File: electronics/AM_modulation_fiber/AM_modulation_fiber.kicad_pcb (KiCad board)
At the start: 2 copper layers, 88.9 x 70.1 mm, 4 parts

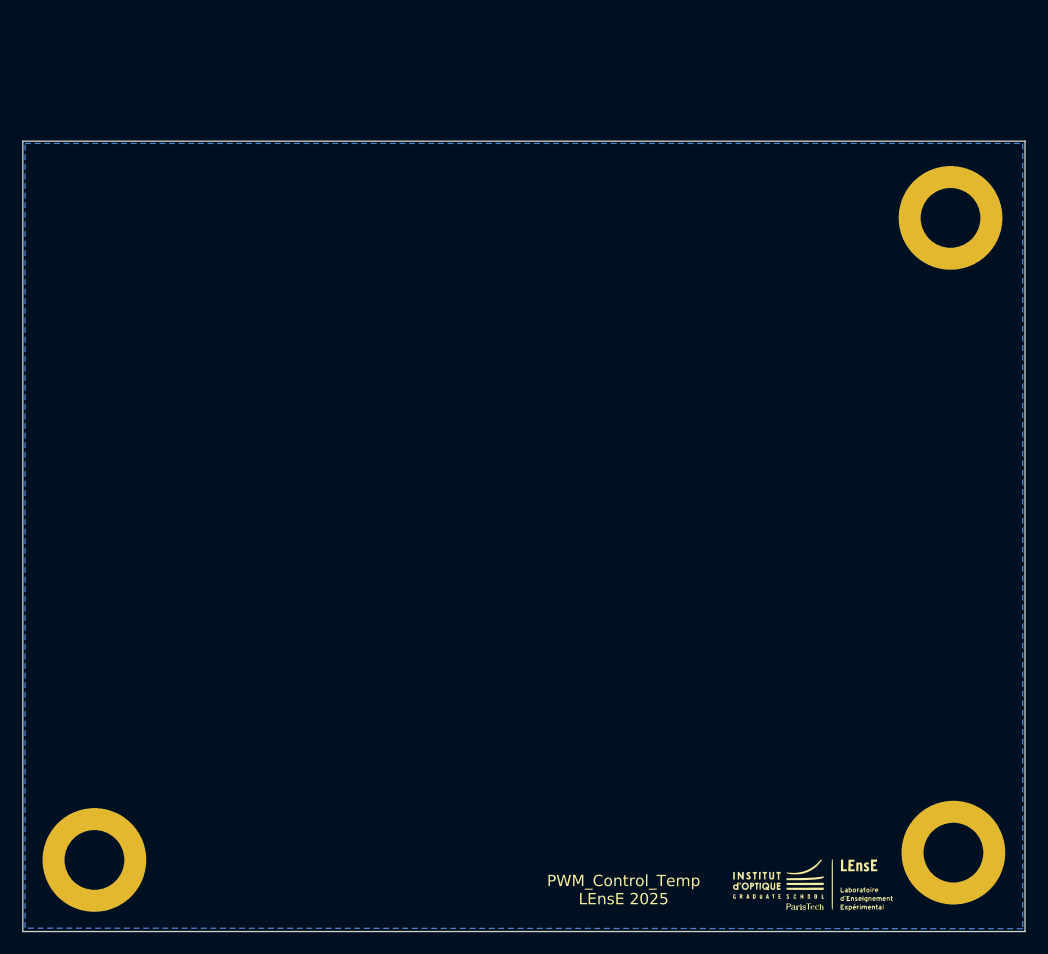
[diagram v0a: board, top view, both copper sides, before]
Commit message: Update AM Modulation and Fiber transmission / demo and labwork
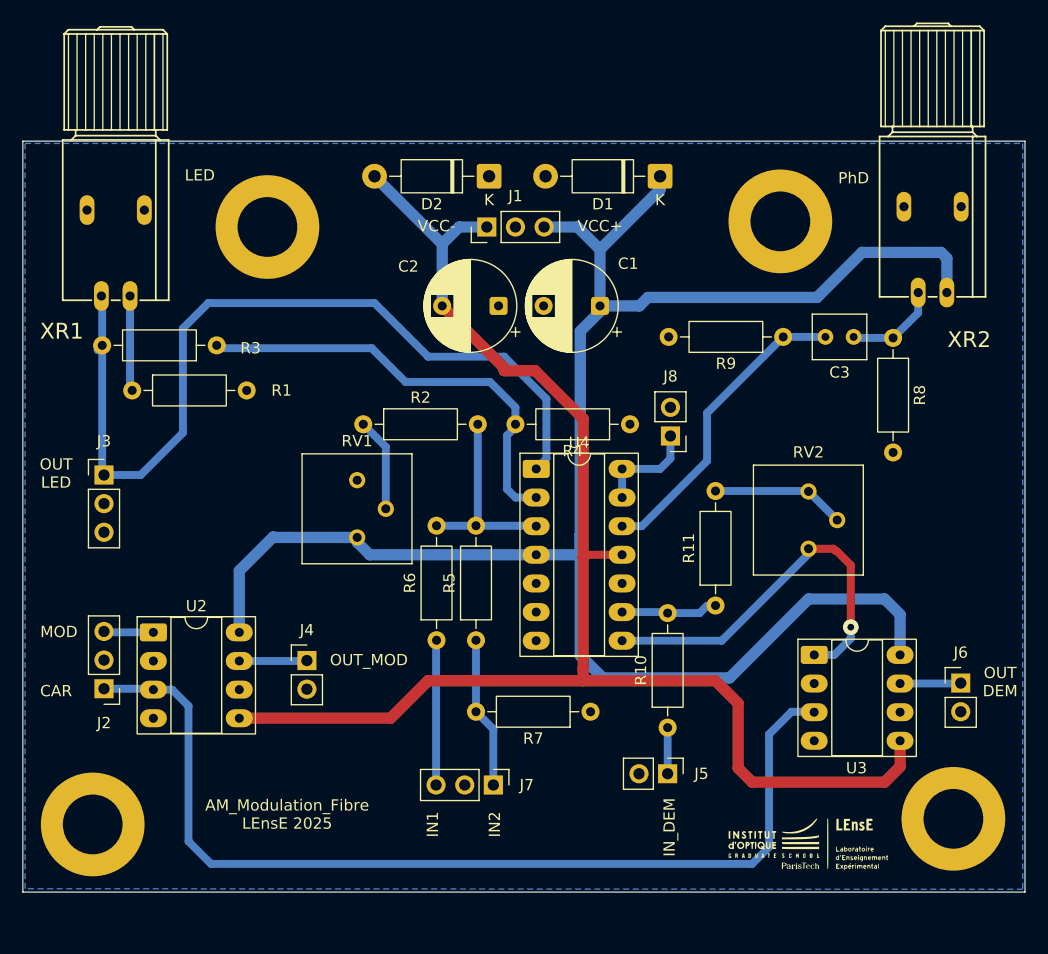
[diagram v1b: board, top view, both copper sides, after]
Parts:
- added ?: , , F.Cu at (199.5, 92.5)
- added C1: 10u, Capacitor_THT:CP_Radial_D8.0mm_P5.00mm, F.Cu at (229.0, 99.5)
- added C2: 10u, Capacitor_THT:CP_Radial_D8.0mm_P5.00mm, F.Cu at (220.0, 99.5)
- added C3: 1u, Capacitor_THT:C_Rect_L4.6mm_W3.8mm_P2.50mm_MKS02_FKP02, F.Cu at (251.5, 102.2)
- added D1: 1N4001, Diode_THT:D_DO-41_SOD81_P10.16mm_Horizontal, F.Cu at (234.3, 88.0)
- added D2: 1N4001, Diode_THT:D_DO-41_SOD81_P10.16mm_Horizontal, F.Cu at (219.2, 88.0)
- added J1: Alim_VCC, Connector_PinHeader_2.54mm:PinHeader_1x03_P2.54mm_Vertical, F.Cu at (219.0, 92.5)
- added J2: Mod_In, Connector_PinHeader_2.54mm:PinHeader_1x03_P2.54mm_Vertical, F.Cu at (185.0, 133.5)
- added J3: Mod_In, Connector_PinHeader_2.54mm:PinHeader_1x03_P2.54mm_Vertical, F.Cu at (185.0, 114.5)
- added J4: OUT_MOD, Connector_PinHeader_2.54mm:PinHeader_1x02_P2.54mm_Vertical, F.Cu at (203.0, 131.0)
- added J5: IN_DEM, Connector_PinHeader_2.54mm:PinHeader_1x02_P2.54mm_Vertical, F.Cu at (235.0, 141.0)
- added J6: OUT_DEM, Connector_PinHeader_2.54mm:PinHeader_1x02_P2.54mm_Vertical, F.Cu at (261.0, 133.0)
- added J7: LED_in, Connector_PinHeader_2.54mm:PinHeader_1x03_P2.54mm_Vertical, F.Cu at (219.5, 142.0)
- added J8: OUT_PHD, Connector_PinHeader_2.54mm:PinHeader_1x02_P2.54mm_Vertical, F.Cu at (235.2, 111.0)
- added R1: 180, Resistor_THT:R_Axial_DIN0207_L6.3mm_D2.5mm_P10.16mm_Horizontal, F.Cu at (187.5, 107.0)
- added R10: 12k, Resistor_THT:R_Axial_DIN0207_L6.3mm_D2.5mm_P10.16mm_Horizontal, F.Cu at (235.0, 136.9)
- added R11: 12k, Resistor_THT:R_Axial_DIN0207_L6.3mm_D2.5mm_P10.16mm_Horizontal, F.Cu at (239.2, 126.1)
- added R2: 47k, Resistor_THT:R_Axial_DIN0207_L6.3mm_D2.5mm_P10.16mm_Horizontal, F.Cu at (208.0, 110.0)
- added R3: 47k, Resistor_THT:R_Axial_DIN0207_L6.3mm_D2.5mm_P10.16mm_Horizontal, F.Cu at (195.0, 103.0)
- added R4: 47k, Resistor_THT:R_Axial_DIN0207_L6.3mm_D2.5mm_P10.16mm_Horizontal, F.Cu at (231.7, 110.0)
- added R5: 47k, Resistor_THT:R_Axial_DIN0207_L6.3mm_D2.5mm_P10.16mm_Horizontal, F.Cu at (218.0, 129.2)
- added R6: 47k, Resistor_THT:R_Axial_DIN0207_L6.3mm_D2.5mm_P10.16mm_Horizontal, F.Cu at (214.5, 129.2)
- added R7: 1k, Resistor_THT:R_Axial_DIN0207_L6.3mm_D2.5mm_P10.16mm_Horizontal, F.Cu at (228.2, 135.5)
- added R8: 120k, Resistor_THT:R_Axial_DIN0207_L6.3mm_D2.5mm_P10.16mm_Horizontal, F.Cu at (255.0, 102.3)
- added R9: 680k, Resistor_THT:R_Axial_DIN0207_L6.3mm_D2.5mm_P10.16mm_Horizontal, F.Cu at (245.2, 102.2)
- added RV1: 1k, Potentiometer_THT:Potentiometer_Bourns_3386P_Vertical, F.Cu at (207.5, 120.0)
- added RV2: 100k, Potentiometer_THT:Potentiometer_Bourns_3386P_Vertical, F.Cu at (247.5, 121.0)
- added U2: AD633ANZ, Package_DIP:DIP-8_W7.62mm_Socket_LongPads, F.Cu at (189.4, 128.5)
- added U3: AD633ANZ, Package_DIP:DIP-8_W7.62mm_Socket_LongPads, F.Cu at (248.0, 130.5)
- added U4: TL084, Package_DIP:DIP-14_W7.62mm_Socket_LongPads, F.Cu at (223.3, 114.0)
- added XR1: SFH756V - LED, SFH250V:SFH-V, F.Cu at (186.0, 91.0)
- added XR2: SFH250V, SFH250V:SFH-V, F.Cu at (258.5, 90.7)
- moved ? 15.1 mm to (245.0, 92.0)
- moved G*** 3.64 mm to (247.5, 147.0)
- moved REF** 3.15 mm to (184.0, 145.5)
- moved REF** 3.00 mm to (260.4, 145.0)
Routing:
- net VCC+: track 0.00 -> 163.1 mm
- net VCC-: track 0.00 -> 132.1 mm
- net IN_CAR: track 0.00 -> 87.9 mm
- net OUT_LED: track 0.00 -> 77.3 mm
- net Net-(U4A--): track 0.00 -> 39.2 mm
- net Net-(U3-X1): track 0.00 -> 34.9 mm, vias 0 -> 1
- net Net-(U4D-+): track 0.00 -> 27.5 mm
- net Net-(U4A-+): track 0.00 -> 18.0 mm
- net IN_2: track 0.00 -> 13.5 mm
- net IN_1: track 0.00 -> 12.9 mm
- net Net-(R11-Pad2): track 0.00 -> 11.9 mm
- net OUT_PHD: track 0.00 -> 9.21 mm
- net I_LED: track 0.00 -> 8.46 mm
- net Offset: track 0.00 -> 8.33 mm
- net VS_PHD: track 0.00 -> 8.11 mm
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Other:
- board size 88.9 x 70.1 mm -> 88.9 x 66.6 mm
- board text added: "AM_Modulation_Fibre LEnsE 2025"
- board text added: "CAR"
- board text added: "IN1"
- board text added: "IN2"
- board text added: "IN_DEM"
- board text added: "LED"
- board text added: "MOD"
- board text added: "OUT DEM"
- board text added: "OUT LED"
- board text added: "OUT_MOD"
- board text added: "PhD"
- board text added: "VCC+"
- board text added: "VCC-"
- board text removed: "PWM_Control_Temp LEnsE 2025"

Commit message: Update AM_Modulation_Fiber circuit
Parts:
- added J9: Mod_In, Connector_PinHeader_2.54mm:PinHeader_1x03_P2.54mm_Vertical, F.Cu at (183.0, 87.5)
- C1, C2: footprint Capacitor_THT:CP_Radial_D8.0mm_P5.00mm -> Capacitor_THT:CP_Radial_D6.3mm_P2.50mm
- C3: footprint Capacitor_THT:C_Rect_L4.6mm_W3.8mm_P2.50mm_MKS02_FKP02 -> Capacitor_THT:C_Rect_L7.0mm_W4.5mm_P5.00mm
- moved C1 2.55 mm to (226.5, 99.0)
- moved C3 2.51 mm to (254.0, 102.5)
- moved R8 2.00 mm to (257.0, 102.3)
- moved C2 1.12 mm to (219.0, 99.0)
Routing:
- net VCC+: track 163.1 -> 214.5 mm
- net OUT_LED: track 77.3 -> 97.0 mm
- net VCC-: track 132.1 -> 130.5 mm
- net VS_PHD: track 8.11 -> 7.32 mm

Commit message: Update AM_Modulation_Fiber
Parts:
- J3: value Mod_In -> PhD_OUT
- J8: value OUT_PHD -> OUT_LED
- moved J3 74.5 mm to (259.5, 113.1), turned to 180 degrees
- moved J8 50.4 mm to (185.0, 114.5), turned to 0 degrees
- moved R8 6.41 mm to (254.0, 108.0), turned to 180 degrees
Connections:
- J3 pad 1: OUT_LED -> OUT_PHD
- J3 pad 3: unconnected-(J3-Pin_3-Pad3) -> VS_PHD
- J8 pad 1: OUT_PHD -> OUT_LED
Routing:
- net OUT_PHD: track 9.21 -> 32.3 mm
- net VS_PHD: track 7.32 -> 16.7 mm
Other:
- board text added: "OUT PHD"
- board text added: "V_PHD"

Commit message: Update AM_Modulation_Fiber
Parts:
- moved RV1 3.66 mm to (204.0, 121.3)
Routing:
- net VCC+: track 214.5 -> 213.2 mm
- net Offset: track 8.33 -> 9.49 mm
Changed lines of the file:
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@@
 	(footprint "Potentiometer_THT:Potentiometer_Bourns_3386P_Vertical"
 		(layer "F.Cu")
-		(at 207.46 120.04)
+		(at 204.015 121.29)
 		(descr "Potentiometer, vertical, Bourns 3386P, https://www.bourns.com/pdfs/3386.pdf")
 		(tags "Potentiometer vertical Bourns 3386P")
@@
 		(tags "Resistor Axial_DIN0207 series Axial Horizontal pin pitch 10.16mm 0.25W = 1/4W length 6.3mm diameter 2.5mm")
 		(property "Reference" "R2"
-			(at 5.08 -2.37 0)
+			(at 0 -2.5 0)
 			(layer "F.SilkS")
 			(effects
@@
 		(tags "Resistor Axial_DIN0207 series Axial Horizontal pin pitch 10.16mm 0.25W = 1/4W length 6.3mm diameter 2.5mm")
 		(property "Reference" "R4"
-			(at 5.08 -2.37 0)
+			(at 0.16 2.5 0)
 			(layer "F.SilkS")
 			(effects
@@
 		(tags "THT DIP DIL PDIP 2.54mm 7.62mm 300mil Socket LongPads")
 		(property "Reference" "U4"
-			(at 3.81 -2.33 0)
+			(at -0.09 17.79 0)
 			(layer "F.SilkS")
 			(effects
@@
 	)
 	(segment
+		(start 208.58 121.58)
+		(end 223.34 121.58)
+		(width 1)
+		(layer "B.Cu")
+		(net 2)
+	)
+	(segment
 		(start 224.04 92.5)
 		(end 227 92.5)
@@
 	)
 	(segment
-		(start 226.75 99)
-		(end 226.5 99)
+		(start 201.25 121.25)
+		(end 201.29 121.29)
 		(width 1)
 		(layer "B.Cu")
@@
 	)
 	(segment
-		(start 229.25 132.5)
-		(end 240.5 132.5)
+		(start 226.75 99)
+		(end 226.5 99)
 		(width 1)
 		(layer "B.Cu")
@@
 	)
 	(segment
-		(start 223.34 121.58)
-		(end 208.58 121.58)
+		(start 229.25 132.5)
+		(end 240.5 132.5)
 		(width 1)
 		(layer "B.Cu")
@@
 	)
 	(segment
-		(start 200.04 120.04)
-		(end 207.46 120.04)
-		(width 1)
-		(layer "B.Cu")
-		(net 2)
-	)
-	(segment
-		(start 207.46 120.46)
-		(end 207.46 120.04)
-		(width 1)
-		(layer "B.Cu")
-		(net 2)
-	)
-	(segment
-		(start 208.58 121.58)
-		(end 207.46 120.46)
+		(start 208.29 121.29)
+		(end 208.58 121.58)
 		(width 1)
 		(layer "B.Cu")
@@
 	)
 	(segment
-		(start 200 120)
-		(end 200.04 120.04)
+		(start 234.33 89.17)
+		(end 234.33 88)
 		(width 1)
 		(layer "B.Cu")
@@
 	)
 	(segment
-		(start 197 128.46)
-		(end 197 123)
+		(start 240.5 132.5)
+		(end 247.5 125.5)
 		(width 1)
 		(layer "B.Cu")
@@
 	)
 	(segment
-		(start 234.33 89.17)
-		(end 234.33 88)
+		(start 201.29 121.29)
+		(end 208.29 121.29)
 		(width 1)
 		(layer "B.Cu")
@@
 	)
 	(segment
-		(start 240.5 132.5)
-		(end 247.5 125.5)
+		(start 229 94.5)
+		(end 234.33 89.17)
 		(width 1)
 		(layer "B.Cu")
@@
 	)
 	(segment
-		(start 229 94.5)
-		(end 234.33 89.17)
+		(start 197 123)
+		(end 198.75 121.25)
 		(width 1)
 		(layer "B.Cu")
@@
 	)
 	(segment
-		(start 197 123)
-		(end 200 120)
+		(start 197 128.46)
+		(end 197 123)
+		(width 1)
+		(layer "B.Cu")
+		(net 2)
+	)
+	(segment
+		(start 198.75 121.25)
+		(end 201.25 121.25)
 		(width 1)
 		(layer "B.Cu")
@@
 	)
 	(segment
-		(start 210 117.5)
-		(end 210 112)
+		(start 206.75 118.555)
+		(end 206.75 111)
 		(width 0.7)
 		(layer "B.Cu")
@@
 	)
 	(segment
-		(start 210 112)
+		(start 206.75 111)
+		(end 207.75 110)
+		(width 0.7)
+		(layer "B.Cu")
+		(net 14)
+	)
+	(segment
+		(start 207.75 110)
 		(end 208 110)
 		(width 0.7)
 		(layer "B.Cu")
+		(net 14)
+	)
+	(segment
+		(start 206.555 118.75)
+		(end 206.75 118.555)
+		(width 0.7)
+		(layer "B.Cu")
